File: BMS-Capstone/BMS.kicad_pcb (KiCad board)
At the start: 2 copper layers, 32 parts, among them IC1 MP2643, IC2 MP2643, Q1 FODM121, Q2 FODM121, Q3 FODM121, Q4 FODM121

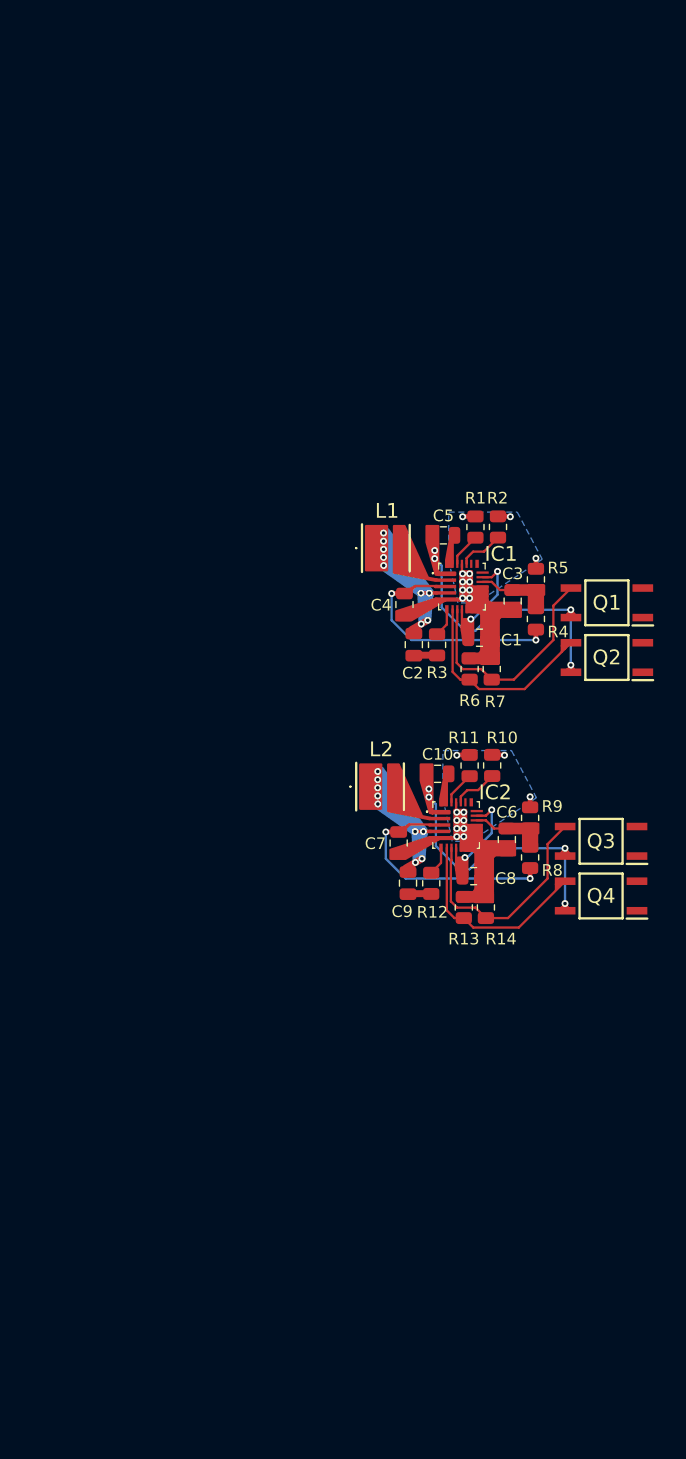
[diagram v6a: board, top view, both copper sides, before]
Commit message: Copied balancer circuit onto pcb
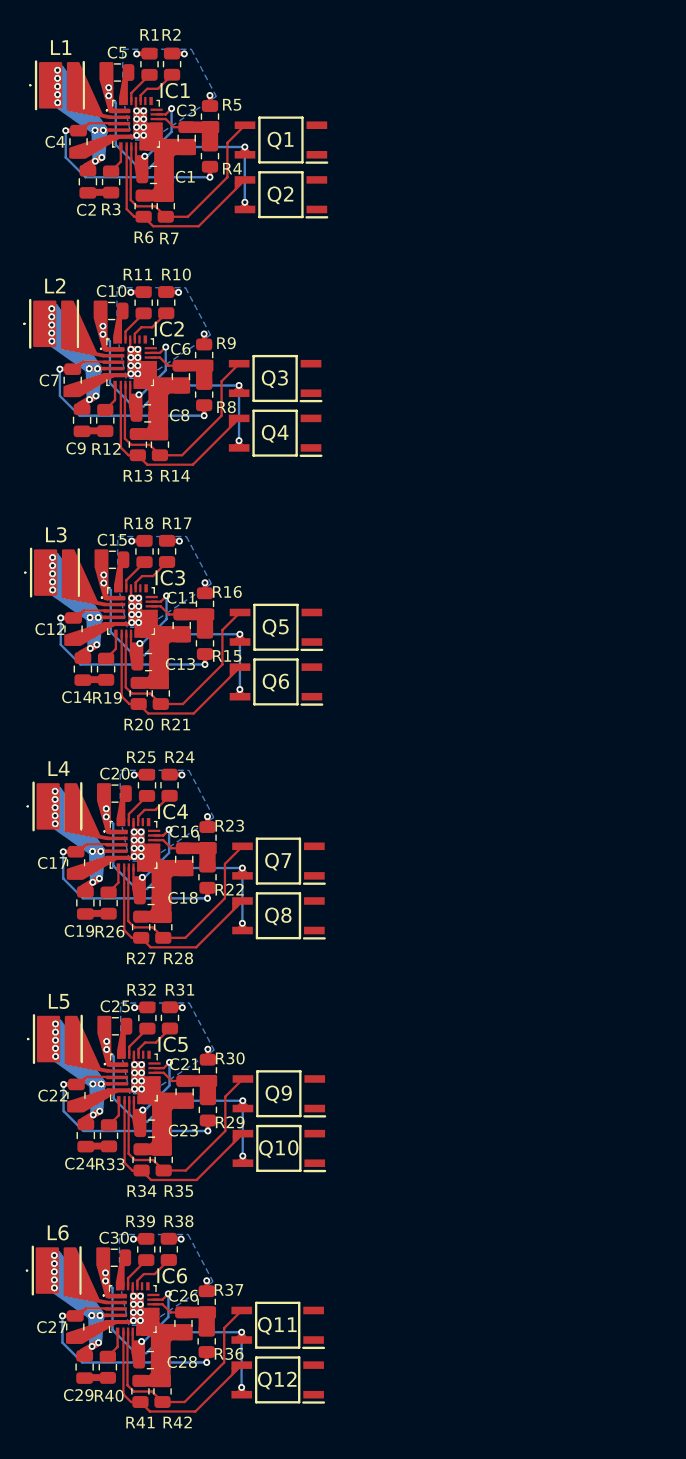
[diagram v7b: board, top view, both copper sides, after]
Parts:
- added C11: C, Capacitor_SMD:C_0805_2012Metric, F.Cu at (128.1, 82.0)
- added C12: C, Capacitor_SMD:C_0805_2012Metric, F.Cu at (118.8, 82.3)
- added C13: C, Capacitor_SMD:C_0805_2012Metric, F.Cu at (125.2, 85.1)
- added C14: C, Capacitor_SMD:C_0805_2012Metric, F.Cu at (119.6, 85.7)
- added C15: C, Capacitor_SMD:C_0805_2012Metric, F.Cu at (122.1, 76.3)
- added C16: C, Capacitor_SMD:C_0805_2012Metric, F.Cu at (128.3, 102.1)
- added C17: C, Capacitor_SMD:C_0805_2012Metric, F.Cu at (119.0, 102.4)
- added C18: C, Capacitor_SMD:C_0805_2012Metric, F.Cu at (125.4, 105.2)
- added C19: C, Capacitor_SMD:C_0805_2012Metric, F.Cu at (119.8, 105.8)
- added C20: C, Capacitor_SMD:C_0805_2012Metric, F.Cu at (122.3, 96.4)
- added C21: C, Capacitor_SMD:C_0805_2012Metric, F.Cu at (128.3, 122.1)
- added C22: C, Capacitor_SMD:C_0805_2012Metric, F.Cu at (119.0, 122.4)
- added C23: C, Capacitor_SMD:C_0805_2012Metric, F.Cu at (125.5, 125.2)
- added C24: C, Capacitor_SMD:C_0805_2012Metric, F.Cu at (119.8, 125.8)
- added C25: C, Capacitor_SMD:C_0805_2012Metric, F.Cu at (122.4, 116.4)
- added C26: C, Capacitor_SMD:C_0805_2012Metric, F.Cu at (128.2, 142.0)
- added C27: C, Capacitor_SMD:C_0805_2012Metric, F.Cu at (118.9, 142.3)
- added C28: C, Capacitor_SMD:C_0805_2012Metric, F.Cu at (125.4, 145.1)
- added C29: C, Capacitor_SMD:C_0805_2012Metric, F.Cu at (119.7, 145.7)
- added C30: C, Capacitor_SMD:C_0805_2012Metric, F.Cu at (122.3, 136.3)
- added IC3: MP2643, SamacSys_Parts:MP2639AGRZ, F.Cu at (123.7, 80.7)
- added IC4: MP2643, SamacSys_Parts:MP2639AGRZ, F.Cu at (123.9, 100.8)
- added IC5: MP2643, SamacSys_Parts:MP2639AGRZ, F.Cu at (123.9, 120.8)
- added IC6: MP2643, SamacSys_Parts:MP2639AGRZ, F.Cu at (123.8, 140.7)
- added L3: L, SamacSys_Parts:MPLAL4020R47 Inductor, F.Cu at (117.2, 77.4)
- added L4: L, SamacSys_Parts:MPLAL4020R47 Inductor, F.Cu at (117.4, 97.5)
- added L5: L, SamacSys_Parts:MPLAL4020R47 Inductor, F.Cu at (117.4, 117.5)
- added L6: L, SamacSys_Parts:MPLAL4020R47 Inductor, F.Cu at (117.3, 137.4)
- added Q10: FODM121, SamacSys_Parts:SOP254P675X240-4N, F.Cu at (136.4, 126.9)
- added Q11: FODM121, SamacSys_Parts:SOP254P675X240-4N, F.Cu at (136.3, 142.1)
- added Q12: FODM121, SamacSys_Parts:SOP254P675X240-4N, F.Cu at (136.3, 146.8)
- added Q5: FODM121, SamacSys_Parts:SOP254P675X240-4N, F.Cu at (136.2, 82.1)
- added Q6: FODM121, SamacSys_Parts:SOP254P675X240-4N, F.Cu at (136.2, 86.8)
- added Q7: FODM121, SamacSys_Parts:SOP254P675X240-4N, F.Cu at (136.4, 102.2)
- added Q8: FODM121, SamacSys_Parts:SOP254P675X240-4N, F.Cu at (136.4, 106.9)
- added Q9: FODM121, SamacSys_Parts:SOP254P675X240-4N, F.Cu at (136.4, 122.2)
- added R15: R, Resistor_SMD:R_0805_2012Metric, F.Cu at (130.1, 83.5)
- added R16: R, Resistor_SMD:R_0805_2012Metric, F.Cu at (130.1, 80.1)
- added R17: 0, Resistor_SMD:R_0805_2012Metric, F.Cu at (126.8, 75.6)
- added R18: R, Resistor_SMD:R_0805_2012Metric, F.Cu at (124.9, 75.6)
- added R19: R, Resistor_SMD:R_0805_2012Metric, F.Cu at (121.6, 85.7)
- added R20: R, Resistor_SMD:R_0805_2012Metric, F.Cu at (124.4, 87.8)
- added R21: R, Resistor_SMD:R_0805_2012Metric, F.Cu at (126.3, 87.8)
- added R22: R, Resistor_SMD:R_0805_2012Metric, F.Cu at (130.3, 103.6)
- added R23: R, Resistor_SMD:R_0805_2012Metric, F.Cu at (130.3, 100.2)
- added R24: 0, Resistor_SMD:R_0805_2012Metric, F.Cu at (127.0, 95.7)
- added R25: R, Resistor_SMD:R_0805_2012Metric, F.Cu at (125.1, 95.7)
- added R26: R, Resistor_SMD:R_0805_2012Metric, F.Cu at (121.8, 105.8)
- added R27: R, Resistor_SMD:R_0805_2012Metric, F.Cu at (124.6, 107.9)
- added R28: R, Resistor_SMD:R_0805_2012Metric, F.Cu at (126.5, 107.9)
- added R29: R, Resistor_SMD:R_0805_2012Metric, F.Cu at (130.3, 123.6)
- added R30: R, Resistor_SMD:R_0805_2012Metric, F.Cu at (130.3, 120.2)
- added R31: 0, Resistor_SMD:R_0805_2012Metric, F.Cu at (127.0, 115.7)
- added R32: R, Resistor_SMD:R_0805_2012Metric, F.Cu at (125.1, 115.7)
- added R33: R, Resistor_SMD:R_0805_2012Metric, F.Cu at (121.8, 125.8)
- added R34: R, Resistor_SMD:R_0805_2012Metric, F.Cu at (124.6, 127.9)
- added R35: R, Resistor_SMD:R_0805_2012Metric, F.Cu at (126.5, 127.9)
- added R36: R, Resistor_SMD:R_0805_2012Metric, F.Cu at (130.2, 143.5)
- added R37: R, Resistor_SMD:R_0805_2012Metric, F.Cu at (130.2, 140.1)
- added R38: 0, Resistor_SMD:R_0805_2012Metric, F.Cu at (126.9, 135.6)
- added R39: R, Resistor_SMD:R_0805_2012Metric, F.Cu at (125.0, 135.6)
- added R40: R, Resistor_SMD:R_0805_2012Metric, F.Cu at (121.7, 145.7)
- added R41: R, Resistor_SMD:R_0805_2012Metric, F.Cu at (124.5, 147.8)
- added R42: R, Resistor_SMD:R_0805_2012Metric, F.Cu at (126.4, 147.8)
- moved C1 48.7 mm to (125.6, 43.2)
- moved C10 48.7 mm to (122.0, 54.9)
- moved C5 48.7 mm to (122.5, 34.4)
- moved C8 48.7 mm to (125.1, 63.7)
- moved R1 48.7 mm to (125.3, 33.7)
- moved R11 48.7 mm to (124.8, 54.2)
- moved R13 48.7 mm to (124.3, 66.4)
- moved R4 48.7 mm to (130.5, 41.6)
- moved R5 48.7 mm to (130.5, 38.2)
- moved R6 48.7 mm to (124.8, 45.9)
- moved R8 48.7 mm to (130.0, 62.1)
- moved R9 48.7 mm to (130.0, 58.7)
- moved C2 48.7 mm to (120.0, 43.8)
- moved C3 48.7 mm to (128.5, 40.1)
- moved C4 48.7 mm to (119.2, 40.4)
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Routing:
- net /BMS Board/3Upper: track 0.00 -> 47.8 mm, vias 0 -> 17
- net /BMS Board/4Upper: track 0.00 -> 47.8 mm, vias 0 -> 17
- net /BMS Board/5Upper: track 0.00 -> 41.3 mm, vias 0 -> 6
- net /BMS Board/2Upper: track 17.5 -> 47.8 mm, vias 2 -> 17
- net Net-(IC3-MODE): track 0.00 -> 20.0 mm
- net Net-(IC6-MODE): track 0.00 -> 20.0 mm
- net Net-(IC5-MODE): track 0.00 -> 20.0 mm
- net Net-(IC4-MODE): track 0.00 -> 20.0 mm
- net Net-(IC6-EN): track 0.00 -> 17.8 mm
- net Net-(IC5-EN): track 0.00 -> 17.8 mm
- net Net-(IC4-EN): track 0.00 -> 17.8 mm
- net Net-(IC3-EN): track 0.00 -> 17.8 mm
- net /BMS Board/6Upper: track 0.00 -> 17.5 mm, vias 0 -> 2
- net /BMS Board/VCC6: track 0.00 -> 8.83 mm
- net /BMS Board/VCC3: track 0.00 -> 8.83 mm
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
